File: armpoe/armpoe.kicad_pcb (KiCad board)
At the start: 2 copper layers, 60 x 60 mm, 108 parts, among them J101 RJ45, Q101 Si4848DY, Q102 Si4848DY, Q103 Si4848DY, Q104 Si2325DS, T101 H2019, T102 HA3691-AL, U101 PM8803, U102 OPTO-TRANSISTOR, U103 TS431, U201 STM32F107XXX-LQFP64, U202 KSZ8001S, U203 MCP1603, X202 CRYSTAL

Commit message: looks to be a complete board, pending a check with the BOM and a good look-over
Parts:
- added MICROUSB-B-ZX62-B-5PA: VAL**, MICROUSB-B-ZX62-B-5PA, B.Cu at (256.0, 97.0)
- moved R125 0.40 mm to (199.0, 110.5), turned to 180 degrees
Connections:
- C104 pad 2: /RTN -> /MCU/Unisolated 48 -
- C105 pad 1: /RTN -> /MCU/Unisolated 48 -
- C106 pad 2: /RTN -> /MCU/Unisolated 48 -
- C107 pad 1: /48V+ filtered input -> /MCU/Unisolated 48 +
- C107 pad 2: /RTN -> /MCU/Unisolated 48 -
- C108 pad 1: /48V+ filtered input -> /MCU/Unisolated 48 +
- C108 pad 2: /RTN -> /MCU/Unisolated 48 -
- C110 pad 2: /RTN -> /MCU/Unisolated 48 -
- C112 pad 1: /RTN -> /MCU/Unisolated 48 -
- D110 pad 1: /RTN -> /MCU/Unisolated 48 -
- D116 pad 2: /RTN -> /MCU/Unisolated 48 -
- JP201 pad A13: (no net) -> /MCU/A13
- JP201 pad A14: (no net) -> /MCU/A14
- JP201 pad A15: (no net) -> /MCU/A15
- JP201 pad A16: (no net) -> /MCU/A16
- JP201 pad A17: (no net) -> /MCU/A17
- JP201 pad A18: (no net) -> /MCU/A18
- JP201 pad A19: (no net) -> /MCU/A19
- JP201 pad A20: (no net) -> /MCU/A20
- JP201 pad A21: (no net) -> /MCU/A21
- JP201 pad A22: (no net) -> /MCU/A22
- JP201 pad A23: (no net) -> /MCU/A23
- JP201 pad A24: (no net) -> /MCU/A24
- JP201 pad A25: (no net) -> /MCU/A25
- JP201 pad A26: (no net) -> /MCU/A26
- JP201 pad A27: (no net) -> /MCU/A27
- JP201 pad A28: (no net) -> /MCU/A28
- JP201 pad A29: (no net) -> /MCU/A29
- JP201 pad A3: (no net) -> /MCU/Unisolated 48 -
- JP201 pad A30: (no net) -> /MCU/A30
- JP201 pad A31: (no net) -> /MCU/A31
- JP201 pad A32: (no net) -> /MCU/A32
- JP201 pad A4: (no net) -> /MCU/Unisolated 48 -
- JP201 pad A6: (no net) -> /MCU/Unisolated 48 +
- JP201 pad A7: (no net) -> /MCU/Unisolated 48 +
- JP201 pad B10: (no net) -> +5V
- JP201 pad B11: (no net) -> +5V
- JP201 pad B12: (no net) -> /MCU/B12
- JP201 pad B13: (no net) -> /MCU/B13
- JP201 pad B14: (no net) -> /MCU/B14
- JP201 pad B15: (no net) -> /MCU/B15
- JP201 pad B16: (no net) -> /MCU/B16
- JP201 pad B17: (no net) -> /MCU/B17
- JP201 pad B18: (no net) -> /MCU/B18
- JP201 pad B19: (no net) -> /MCU/B19
- JP201 pad B20: (no net) -> /MCU/B20
- JP201 pad B21: (no net) -> /MCU/B21
- JP201 pad B22: (no net) -> /MCU/B22
- JP201 pad B23: (no net) -> /MCU/B23
- JP201 pad B24: (no net) -> /MCU/B24
- JP201 pad B25: (no net) -> /MCU/B25
- JP201 pad B26: (no net) -> /MCU/B26
- JP201 pad B27: (no net) -> /MCU/B27
- JP201 pad B28: (no net) -> /MCU/B28
- JP201 pad B29: (no net) -> /MCU/B29
- JP201 pad B30: (no net) -> /MCU/B30
- JP201 pad B31: (no net) -> /MCU/B31
- JP201 pad B32: (no net) -> /MCU/B32
- JP201 pad B6: (no net) -> GND
- JP201 pad B7: (no net) -> GND
- JP201 pad B8: (no net) -> +3.3V
- JP201 pad B9: (no net) -> +3.3V
- L101 pad 2: /48V+ filtered input -> /MCU/Unisolated 48 +
- Q104 pad S: /RTN -> /MCU/Unisolated 48 -
- R103 pad 1: /48V+ filtered input -> /MCU/Unisolated 48 +
- R108 pad 1: /RTN -> /MCU/Unisolated 48 -
- R112 pad 1: /RTN -> /MCU/Unisolated 48 -
- R116 pad 2: /RTN -> /MCU/Unisolated 48 -
- R121 pad 1: /RTN -> /MCU/Unisolated 48 -
- T102 pad 1: /48V+ filtered input -> /MCU/Unisolated 48 +
- T102 pad 5: /RTN -> /MCU/Unisolated 48 -
- U101 pad 11: /48V+ filtered input -> /MCU/Unisolated 48 +
- U101 pad 12: /48V+ filtered input -> /MCU/Unisolated 48 +
- U101 pad 4: /RTN -> /MCU/Unisolated 48 -
- U101 pad 9: /RTN -> /MCU/Unisolated 48 -
- U201 pad 1: (no net) -> /MCU/A32
- U201 pad 10: (no net) -> /MCU/A26
- U201 pad 11: (no net) -> /MCU/A25
- U201 pad 14: (no net) -> /MCU/A24
- U201 pad 17: (no net) -> /MCU/A23
- U201 pad 2: (no net) -> /MCU/A31
- U201 pad 20: (no net) -> /MCU/A22
- U201 pad 21: (no net) -> /MCU/A21
- U201 pad 22: (no net) -> /MCU/A20
- U201 pad 26: (no net) -> /MCU/A19
- U201 pad 27: (no net) -> /MCU/A18
- U201 pad 28: (no net) -> /MCU/A17
- U201 pad 29: (no net) -> /MCU/A16
- U201 pad 3: (no net) -> /MCU/A30
- U201 pad 35: (no net) -> /MCU/A15
- U201 pad 36: (no net) -> /MCU/A14
- U201 pad 37: (no net) -> /MCU/A13
- U201 pad 38: (no net) -> /MCU/B12
- U201 pad 39: (no net) -> /MCU/B13
- U201 pad 4: (no net) -> /MCU/A29
- U201 pad 40: (no net) -> /MCU/ETH_RST
- U201 pad 42: /MCU/ETH_RST -> /MCU/B14
- U201 pad 43: (no net) -> /MCU/B15
- U201 pad 44: (no net) -> /MCU/B16
- U201 pad 45: (no net) -> /MCU/B17
- U201 pad 46: (no net) -> /MCU/B18
- U201 pad 49: (no net) -> /MCU/B19
- U201 pad 50: (no net) -> /MCU/B20
- U201 pad 51: (no net) -> /MCU/B21
- U201 pad 52: (no net) -> /MCU/B22
- U201 pad 53: (no net) -> /MCU/B23
- U201 pad 54: (no net) -> /MCU/B24
- U201 pad 55: (no net) -> /MCU/B25
- U201 pad 56: (no net) -> /MCU/B26
- U201 pad 57: (no net) -> /MCU/B27
- U201 pad 58: (no net) -> /MCU/B28
- U201 pad 59: (no net) -> /MCU/B29
- U201 pad 60: (no net) -> /MCU/B30
- U201 pad 61: (no net) -> /MCU/B31
- U201 pad 62: (no net) -> /MCU/B32
- U201 pad 7: (no net) -> /MCU/A28
- U201 pad 8: (no net) -> /MCU/A27
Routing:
- net (no net): track 342.7 -> 0.00 mm, vias 19 -> 0
- net /MCU/Unisolated 48 -: track 0.00 -> 141.7 mm, vias 0 -> 7
- net /RTN: track 117.1 -> 0.00 mm, vias 4 -> 0
- net /MCU/Unisolated 48 +: track 0.00 -> 82.2 mm, vias 0 -> 1
- net +3.3V: track 154.9 -> 215.6 mm, vias 12 -> 15
- net GND: track 268.6 -> 312.3 mm, vias 9 -> 16
- net /48V+ filtered input: track 30.1 -> 0.00 mm
- net /MCU/A16: track 0.00 -> 28.5 mm, vias 0 -> 1
- net /MCU/A17: track 0.00 -> 27.8 mm, vias 0 -> 1
- net /MCU/A18: track 0.00 -> 27.5 mm, vias 0 -> 1
- net /MCU/A19: track 0.00 -> 26.5 mm, vias 0 -> 1
- net /MCU/A20: track 0.00 -> 25.5 mm, vias 0 -> 1
- net /MCU/A22: track 0.00 -> 25.2 mm, vias 0 -> 1
- net /MCU/A21: track 0.00 -> 25.2 mm, vias 0 -> 1
- net /MCU/A23: track 0.00 -> 24.7 mm, vias 0 -> 1
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- added copper zone on B.Cu, net +5V
- added copper zone on B.Cu, net /MCU/Unisolated 48 -
- added copper zone on F.Cu, net /MCU/Unisolated 48 -
- added copper zone on B.Cu, net /VSS input
- added copper zone on F.Cu, net /VSS input
- added copper zone on B.Cu, net /primary low
- added copper zone on F.Cu, net /primary low
- added copper zone on B.Cu, net GND
- added copper zone on F.Cu, net GND
- added copper zone on B.Cu, net N-0000021
- added copper zone on F.Cu, net N-0000021
- added copper zone on B.Cu, net N-000004
- added copper zone on F.Cu, net N-000004
- added copper zone on B.Cu, net N-0000058
- added copper zone on F.Cu, net N-0000058
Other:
- net class 48Vuniso added: clearance 0.8, trace_width 0.254, via_dia 0.889, via_drill 0.635

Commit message: swapped passives to match what I can order.
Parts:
- removed C211: 100nF, SM0603
- removed MICROUSB-B-ZX62-B-5PA: VAL**, MICROUSB-B-ZX62-B-5PA
- C120, R101, R102: footprint SM0603 -> SM0805
- R118, R125: footprint SM0805 -> SM0603
- R201, R202: value 220 -> 510
- moved R101 1.75 mm to (191.2, 76.5)
- moved D113 1.27 mm to (203.9, 103.3), turned to 0 degrees
- moved R115 1.25 mm to (204.0, 105.0), turned to 0 degrees
- moved R102 0.25 mm to (194.2, 76.5)
- moved C125 0.21 mm to (212.9, 107.9)
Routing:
- net +3.3V: track 215.6 -> 191.4 mm, vias 15 -> 13
- net /MCU/3.3V: track 3.73 -> 15.1 mm, vias 0 -> 2
- net GND: track 312.3 -> 314.8 mm
- net N-0000043: track 34.8 -> 36.0 mm
- net /48V+ unfiltered input: track 23.3 -> 22.3 mm
- net /VSS input: track 36.2 -> 36.8 mm
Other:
- net class 48Vuniso: clearance 0.8 -> 0.2

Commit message: All routed. Again.
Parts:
- removed C205, C208: 1uF, SM0603
- removed C206, C207: 100nF, SM0603
- added C220: 10uF, SM0805, F.Cu at (238.2, 86.2)
- added C221: 10uF, SM0805, F.Cu at (226.7, 87.2)
- added C222: 10uF, SM0805, F.Cu at (237.5, 75.7)
- added C230: 100nF, SM0603, F.Cu at (236.5, 86.2)
- added C231: 100nF, SM0603, F.Cu at (229.2, 88.2)
- added C232: 100nF, SM0603, F.Cu at (233.7, 75.0)
- added C233: 100nF, SM0603, F.Cu at (235.3, 75.0)
- added C234: 100nF, SM0603, F.Cu at (231.8, 87.7)
- added C235: 100nF, SM0603, F.Cu at (232.1, 75.0)
- U202: value KSZ8001S -> KSZ8041; footprint SSOP48 -> -TQFP48
- moved R204 6.93 mm to (227.5, 74.5), turned to 0 degrees
- moved R210 2.45 mm to (233.8, 70.9), turned to 270 degrees
- moved U202 2.24 mm to (231.9, 81.7), turned to 180 degrees
- moved C203 1.10 mm to (232.3, 70.4)
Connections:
- R201 pad 1: N-0000072 -> N-0000063
- R202 pad 1: N-0000073 -> N-0000062
- U202 pad 1: /MCU/RMII_MDIO -> GND
- U202 pad 10: (no net) -> /MCU/RX+
- U202 pad 11: (no net) -> /MCU/TX-
- U202 pad 12: GND -> /MCU/TX+
- U202 pad 13: +1.8V -> GND
- U202 pad 15: (no net) -> /MCU/MCO_25
- U202 pad 16: /MCU/RMII_TXEN -> (no net)
- U202 pad 17: /MCU/RMII_TX0 -> GND
- U202 pad 18: /MCU/RMII_TX1 -> /MCU/RMII_MDIO
- U202 pad 19: (no net) -> /MCU/RMII_MDC
- U202 pad 2: /MCU/RMII_MDC -> GND
- U202 pad 22: (no net) -> /MCU/RMII_RX1
- U202 pad 23: GND -> /MCU/RMII_RX0
- U202 pad 24: +3.3V -> GND
- U202 pad 25: (no net) -> +3.3V
- U202 pad 26: (no net) -> +3.3V
- U202 pad 27: N-0000073 -> /MCU/RMII_CRX_DV
- U202 pad 28: N-0000072 -> (no net)
- U202 pad 3: (no net) -> GND
- U202 pad 30: (no net) -> GND
- U202 pad 32: /MCU/RX- -> (no net)
- U202 pad 33: /MCU/RX+ -> (no net)
- U202 pad 34: (no net) -> /MCU/RMII_TXEN
- U202 pad 35: GND -> /MCU/RMII_TX0
- U202 pad 36: GND -> /MCU/RMII_TX1
- U202 pad 37: (no net) -> GND
- U202 pad 38: +3.3V -> (no net)
- U202 pad 39: GND -> (no net)
- U202 pad 4: (no net) -> +1.8V
- U202 pad 40: /MCU/TX- -> (no net)
- U202 pad 41: /MCU/TX+ -> (no net)
- U202 pad 42: (no net) -> N-0000062
- U202 pad 43: (no net) -> N-0000063
- U202 pad 44: GND -> (no net)
- U202 pad 46: /MCU/MCO_25 -> (no net)
- U202 pad 47: +1.8V -> /MCU/ETH_RST
- U202 pad 48: /MCU/ETH_RST -> (no net)
- U202 pad 5: /MCU/RMII_RX1 -> +1.8V
- U202 pad 6: /MCU/RMII_RX0 -> +1.8V
- U202 pad 8: GND -> +3.3V
- U202 pad 9: /MCU/RMII_CRX_DV -> /MCU/RX-
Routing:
- net N-0000062: track 0.00 -> 30.8 mm, vias 0 -> 2
- net GND: track 314.8 -> 289.3 mm, vias 16 -> 17
- net N-0000073: track 25.4 -> 0.00 mm, vias 2 -> 0
- net +3.3V: track 191.4 -> 173.8 mm, vias 13 -> 9
- net N-0000063: track 0.00 -> 15.4 mm
- net /MCU/RMII_CRX_DV: track 14.4 -> 27.4 mm, vias 0 -> 2
- net /MCU/ETH_RST: track 37.1 -> 49.6 mm, vias 2 -> 4
- net N-0000072: track 8.06 -> 0.00 mm
- net /MCU/RX+: track 13.9 -> 21.5 mm
- net /MCU/RX-: track 22.4 -> 28.8 mm
- net /MCU/TXCT: track 4.95 -> 10.8 mm
- net /MCU/RMII_TXEN: track 27.0 -> 21.2 mm
- net /MCU/3.3V: track 15.1 -> 20.8 mm, vias 2 -> 0
- net /MCU/MCO_25: track 49.2 -> 43.9 mm
- net /MCU/RMII_MDIO: track 21.9 -> 26.9 mm
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
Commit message: This is what was sent off, I belive. I'm in the process fo fixing the errors now
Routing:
- net /ARTN: track 60.9 -> 61.6 mm
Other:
- board text added: "G"
- board text added: "S"
- board text added: "STM32F107 PoE Board"
- board text added: "Scott Gilliland"
- board text added: "smg.ideacraft.org"

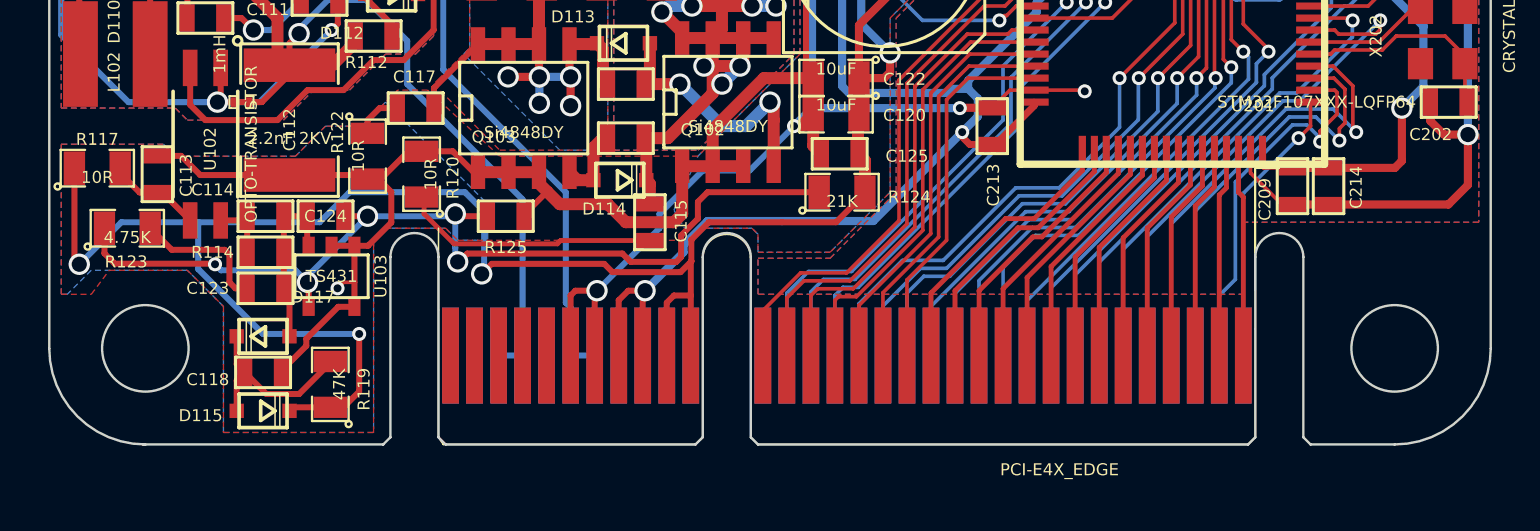
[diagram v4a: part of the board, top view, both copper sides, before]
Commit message: fixed pci express card slot size
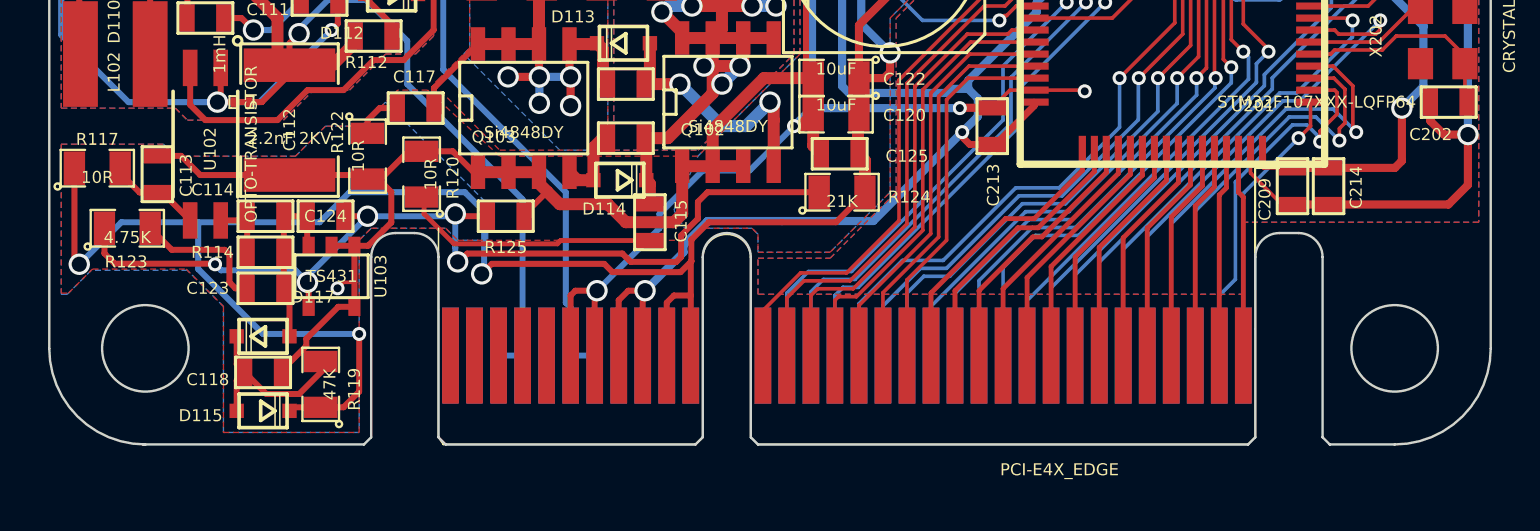
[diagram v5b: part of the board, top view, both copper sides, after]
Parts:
- moved R119 0.40 mm to (191.3, 117.5)
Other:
- outline, holes or cut-outs redrawn
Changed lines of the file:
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@@
     (area 171.532639 59.619499 241.680501 121.55625)
     (thickness 1.6)
-    (drawings 61)
+    (drawings 66)
     (tracks 1742)
     (zones 0)
@@
   (layers
     (15 F.Cu signal)
-    (0 B.Cu signal hide)
+    (0 B.Cu signal)
     (16 B.Adhes user hide)
     (17 F.Adhes user hide)
     (18 B.Paste user hide)
     (19 F.Paste user hide)
-    (20 B.SilkS user)
+    (20 B.SilkS user hide)
     (21 F.SilkS user)
-    (22 B.Mask user)
+    (22 B.Mask user hide)
     (23 F.Mask user)
     (24 Dwgs.User user hide)
@@
   )
   (setup
-    (last_trace_width 2)
+    (last_trace_width 0.1524)
     (user_trace_width 0.1524)
     (user_trace_width 0.2032)
@@
     (zone_45_only yes)
     (trace_min 0.1524)
-    (segment_width 1.96)
+    (segment_width 0.1)
     (edge_width 0.1)
     (via_size 0.889)
@@
   )
   (module SM0805 (layer F.Cu)
-    (at 191.7 117.5 90)
+    (at 191.3 117.5 90)
     (attr smd)
     (fp_text reference R119 (at -0.2 1.4 90) (layer F.SilkS)
@@
     )
   )
+  (gr_line (start 195.2 111.2) (end 194.4 111.2) (angle 90) (layer Edge.Cuts) (width 0.1))
+  (gr_line (start 232 111.2) (end 231.2 111.2) (angle 90) (layer Edge.Cuts) (width 0.1))
+  (gr_arc (start 232 112.2) (end 232 111.2) (angle 90) (layer Edge.Cuts) (width 0.1))
+  (gr_arc (start 195.2 112.2) (end 195.2 111.2) (angle 90) (layer Edge.Cuts) (width 0.1))
+  (gr_line (start 200 125) (end 239 125) (angle 90) (layer Cmts.User) (width 0.1))
   (gr_text S (at 213.2 82.3) (layer B.Mask)
     (effects (font (size 6 6) (thickness 1.2)) (justify mirror))
@@
   (gr_line (start 240 115.7) (end 240 63.5) (angle 90) (layer Dwgs.User) (width 0.761))
   (gr_line (start 241.3 117.5) (end 241.3 115.8) (angle 90) (layer Dwgs.User) (width 0.761))
-  (gr_arc (start 195.2 112.2) (end 194.2 112.2) (angle 180) (layer Edge.Cuts) (width 0.1))
+  (gr_arc (start 194.4 112.2) (end 193.4 112.2) (angle 90) (layer Edge.Cuts) (width 0.1))
   (gr_arc (start 208.2 112.2) (end 207.2 112.2) (angle 180) (layer Edge.Cuts) (width 0.1))
-  (gr_line (start 236 120) (end 232.5 120) (angle 90) (layer Edge.Cuts) (width 0.1))
+  (gr_line (start 236 120) (end 233.3 120) (angle 90) (layer Edge.Cuts) (width 0.1))
   (gr_line (start 196.5 120) (end 206.9 120) (angle 90) (layer Edge.Cuts) (width 0.1))
-  (gr_line (start 193.9 120) (end 183.9 120) (angle 90) (layer Edge.Cuts) (width 0.1))
-  (gr_line (start 194.2 119.7) (end 193.9 120) (angle 90) (layer Edge.Cuts) (width 0.1))
-  (gr_line (start 194.2 119.7) (end 194.2 112.2) (angle 90) (layer Edge.Cuts) (width 0.1))
+  (gr_line (start 193.1 120) (end 183.9 120) (angle 90) (layer Edge.Cuts) (width 0.1))
+  (gr_line (start 193.4 119.7) (end 193.1 120) (angle 90) (layer Edge.Cuts) (width 0.1))
+  (gr_line (start 193.4 119.7) (end 193.4 112.2) (angle 90) (layer Edge.Cuts) (width 0.1))
   (gr_line (start 196.2 119.7) (end 196.2 112.2) (angle 90) (layer Edge.Cuts) (width 0.1))
   (gr_line (start 196.5 120) (end 196.2 119.7) (angle 90) (layer Edge.Cuts) (width 0.1))
@@
   (gr_line (start 206.9 120) (end 207.2 119.7) (angle 90) (layer Edge.Cuts) (width 0.1))
   (gr_line (start 230.2 112.2) (end 230.2 119.7) (angle 90) (layer Edge.Cuts) (width 0.1))
-  (gr_line (start 232.2 119.7) (end 232.5 120) (angle 90) (layer Edge.Cuts) (width 0.1))
-  (gr_line (start 232.2 112.2) (end 232.2 119.7) (angle 90) (layer Edge.Cuts) (width 0.1))
-  (gr_arc (start 231.2 112.2) (end 230.2 112.2) (angle 180) (layer Edge.Cuts) (width 0.1))
+  (gr_line (start 233 119.7) (end 233.3 120) (angle 90) (layer Edge.Cuts) (width 0.1))
+  (gr_line (start 233 112.2) (end 233 119.7) (angle 90) (layer Edge.Cuts) (width 0.1))
+  (gr_arc (start 231.2 112.2) (end 230.2 112.2) (angle 90) (layer Edge.Cuts) (width 0.1))
   (gr_line (start 229.9 120) (end 230.2 119.7) (angle 90) (layer Edge.Cuts) (width 0.1))
   (gr_line (start 196.75 103.25) (end 196.75 98.75) (angle 90) (layer Dwgs.User) (width 1.2))
@@
     (polygon
       (pts
-        (xy 198.25 111.5) (xy 197 111.5) (xy 196.5 111) (xy 194 111) (xy 193.5 111.5)
-        (xy 193.5 119.5) (xy 187.25 119.5) (xy 187.25 114.25) (xy 185.75 112.75) (xy 181.75 112.75)
+        (xy 198.25 111.5) (xy 197 111.5) (xy 196.5 111) (xy 193.4 111) (xy 192.9 111.5)
+        (xy 192.9 119.5) (xy 187.25 119.5) (xy 187.25 114.25) (xy 185.75 112.75) (xy 181.75 112.75)
         (xy 180.75 113.75) (xy 180.5 113.75) (xy 180.5 107.5) (xy 184.75 107.5) (xy 185.25 108)
         (xy 190.25 108) (xy 191.5 106.75) (xy 193 106.75) (xy 194 105.75) (xy 198.25 110)
@@
     (polygon
       (pts
-        (xy 181.75 113.75) (xy 182.5 112.75) (xy 185.75 112.75) (xy 187.25 114.25) (xy 187.25 119.5)
-        (xy 193.5 119.5) (xy 193.5 111.5) (xy 194 111) (xy 196.5 111) (xy 197 111.5)
+        (xy 180.8 113.7) (xy 181.8 112.7) (xy 185.7 112.7) (xy 187.25 114.25) (xy 187.25 119.5)
+        (xy 192.9 119.5) (xy 192.9 111.5) (xy 193.4 111) (xy 196.5 111) (xy 197 111.5)
         (xy 206.75 111.5) (xy 207.25 111) (xy 209.25 111) (xy 209.5 111.25) (xy 209.5 112)
         (xy 212.5 112) (xy 215 109.5) (xy 215 102.25) (xy 221.25 96) (xy 221.25 84.5)
         (xy 218.25 87.5) (xy 211.25 87.5) (xy 211.25 103.75) (xy 207 108) (xy 198.75 108)
         (xy 195.75 105.25) (xy 194.5 105.25) (xy 193 106.75) (xy 191.5 106.75) (xy 190.25 108)
-        (xy 185.25 108) (xy 184.75 107.5) (xy 180.5 107.5) (xy 180.5 113.75)
+        (xy 185.25 108) (xy 184.75 107.5) (xy 180.5 107.5) (xy 180.5 113.7)
       )
     )
